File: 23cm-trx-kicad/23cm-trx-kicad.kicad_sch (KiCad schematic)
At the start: 62 parts, among them J1 LCD BACKLIGHT, J2 LCD I2C, Q1 BC547, Q2 BD138, Q3 BC557, SW1 RotaryEncoder_Switch, U1 ADF4153, U2 L78L09_SOT89, U3 LM741, U4 LM386

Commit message: Further schematic work
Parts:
- added X1: TCXO-13MHz, Oscillator:Oscillator_SMD_Abracon_ASE-4Pin_3.2x2.5mm, symbol Oscillator:ASE-xxxMHz
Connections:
- net GND: now also X1.2 (GND), X1.4 (Vdd)
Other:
- note added: "DRAW SYMBOL FOR MC3362"
- note removed: "DRAW SYMBOL FOR TCXO-13MHZ"
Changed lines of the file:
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@@
 	(wire
 		(pts
+			(xy 144.78 157.48) (xy 146.05 157.48)
+		)
+		(stroke
+			(width 0)
+			(type default)
+		)
+	)
+	(wire
+		(pts
 			(xy 67.31 68.58) (xy 67.31 77.47)
 		)
@@
 		)
 	)
+	(text "DRAW SYMBOL\nFOR MC3362"
+		(exclude_from_sim no)
+		(at 240.03 133.096 0)
+		(effects
+			(font
+				(size 1.27 1.27)
+			)
+		)
+	)
 	(text "POWER\nAMPLIFIER\n(PA)"
 		(exclude_from_sim no)
@@
 		)
 	)
-	(text "DRAW SYMBOL\nFOR TCXO-13MHZ"
-		(exclude_from_sim no)
-		(at 145.796 157.734 0)
-		(effects
-			(font
-				(size 1.27 1.27)
-			)
-		)
-	)
 	(text "USER MENU INPUT"
 		(exclude_from_sim no)
@@
 	(global_label "GND"
 		(shape passive)
+		(at 144.78 172.72 270)
+		(fields_autoplaced yes)
+		(effects
+			(font
+				(size 1.27 1.27)
+			)
+			(justify right)
+		)
+		(property "Intersheetrefs" "${INTERSHEET_REFS}"
+			(at 144.78 178.4644 90)
+			(effects
+				(font
+					(size 1.27 1.27)
+				)
+				(justify right)
+				(hide yes)
+			)
+		)
+	)
+	(global_label "GND"
+		(shape passive)
 		(at 55.88 92.71 270)
 		(fields_autoplaced yes)
@@
 		)
 	)
+	(global_label "GND"
+		(shape passive)
+		(at 146.05 157.48 0)
+		(fields_autoplaced yes)
+		(effects
+			(font
+				(size 1.27 1.27)
+			)
+			(justify left)
+		)
+		(property "Intersheetrefs" "${INTERSHEET_REFS}"
+			(at 151.7944 157.48 0)
+			(effects
+				(font
+					(size 1.27 1.27)
+				)
+				(justify left)
+				(hide yes)
+			)
+		)
+	)
 	(global_label "MCU-AUDIO"
 		(shape output)
@@
 					(unit 1)
 				)
+			)
+		)
+	)
+	(symbol
+		(lib_id "Oscillator:ASE-xxxMHz")
+		(at 144.78 165.1 0)
+		(unit 1)
+		(exclude_from_sim no)
+		(in_bom yes)
+		(on_board yes)
+		(dnp no)
+		(fields_autoplaced yes)
+		(property "Reference" "X1"
+			(at 157.48 158.7814 0)
+			(effects
+				(font
+					(size 1.27 1.27)
+				)
+			)
+		)
+		(property "Value" "TCXO-13MHz"
+			(at 157.48 161.3214 0)
+			(effects
+				(font
+					(size 1.27 1.27)
+				)
+			)
+		)
+		(property "Footprint" "Oscillator:Oscillator_SMD_Abracon_ASE-4Pin_3.2x2.5mm"
+			(at 162.56 173.99 0)
+			(effects
+				(font
+					(size 1.27 1.27)
+				)
+				(hide yes)
+			)
+		)
+		(property "Datasheet" ""
+			(at 142.24 165.1 0)
+			(effects
+				(font
+					(size 1.27 1.27)
+				)
+				(hide yes)
+			)
+		)
+		(property "Description" "3.3V CMOS SMD Crystal Clock Oscillator"
+			(at 144.78 165.1 0)
+			(effects
+				(font
+					(size 1.27 1.27)
+				)
+				(hide yes)
+			)
+		)
+		(pin "4"
+		)
+		(pin "1"
+		)
+		(pin "2"
+		)
+		(pin "3"
+		)
+		(instances
+			(project ""
+				(path "/02f64fd1-78db-4ce7-af00-a5ea9858044e"
+					(reference "X1")
+					(unit 1)
+				)

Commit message: More schematic
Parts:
- added C23: 100nF, symbol Device:C_Small
- added C24: 1nF, symbol Device:C_Small
- added D1: BZX84C3V3, Package_TO_SOT_SMD:SOT-23, symbol Diode:BZX84Cxx
- added R23: 470, symbol Device:R_Small_US
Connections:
- net 13.8V: now also R23.2
- net GND: now also C23.2, C24.2, D1.1 (A)
- net at C15.2, R20.1: now also C24.1
- net at X1.1 (EN): now also C23.1, D1.3 (K), R23.1
- net at X1.3 (OUT): now also C18.2
- net PLL-RF renamed PLL-RF-IN
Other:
- note added: "HOW IT WORKS (I THINK!): - THE OSCILLATOR CRYSTAL GENERATES A REFERENCE 13MHz SIGNAL THAT IS PASSED IN TO ADF4153. - USING AN EXTERNAL LOOP FILTER BETWEEN PINS x AND y, THE ADF4153 IMPLEMENTS A PHASE DETECTOR (PD) THAT COMPARES THE SIGNAL TO THAT RECEIVED ON PIN 6 (RFIN)."
- note added: "OUTPUT AUDIO POWER AMPLIFIER AND SPEAKER"
- note added: "PHASE LOCKED LOOP"
- note removed: "PHASE LOCK LOOP"
- note removed: "POWER AMPLIFIER AND SPEAKER"
- moved on the sheet: C15, C16, C17, C18, C19, C20, C21, C22, R20, R21, R22, SW1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

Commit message: Further schematic work
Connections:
- net at C15.2, C24.1: no longer R20.1
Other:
- note added: "HOW IT WORKS (I THINK!): - THE OSCILLATOR CRYSTAL GENERATES A REFERENCE 13MHz SIGNAL THAT IS PASSED IN TO ADF4153. - THE ADF4153 IS A FRACTIONAL-N FREQUENCY SYNTHESIZER THAT CONTAINS LOCAL OSCILLATORS AND A LOW NOISE DIGITAL FREQUENCY PHASE DETECTOR (PFD) FUNCTIONING AS THE PHASE DETECTOR (PD) WITHIN THE PHASE LOCKED LOOP. IT CHIEFLY COMPARES THE REFERENCE SIGNAL ON PIN 8 (REFIN) TO THAT RECEIVED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"
- note added: "VCO"
- note removed: "HOW IT WORKS (I THINK!): - THE OSCILLATOR CRYSTAL GENERATES A REFERENCE 13MHz SIGNAL THAT IS PASSED IN TO ADF4153. - USING AN EXTERNAL LOOP FILTER BETWEEN PINS x AND y, THE ADF4153 IMPLEMENTS A PHASE DETECTOR (PD) THAT COMPARES THE SIGNAL TO THAT RECEIVED ON PIN 6 (RFIN)."
- moved on the sheet: C10, C11, C15, C16, C17, C18, C19, C20, C21, C22, C23, C24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

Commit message: VCO
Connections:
- net CTCSS-TONE: no longer A1.14 (D11)
- net SPI-SCK: now reaches A1.16 (D13)
- net SPI-SCK: now also U1.11 (CLK)
- net CLK: no longer names the net of A1.19 (A0)
- net CLK: no longer U1.11 (CLK)
- net DAT: no longer names the net of A1.20 (A1)
- net DAT: no longer U1.12 (DATA)
- net LE: no longer names the net of A1.21 (A2)
- net LE: no longer U1.13 (LE)
- net PLL-RF-IN: no longer names the net of U1.6 (RFINA)
- new net SPI-MOSI: A1.14 (D11), U1.12 (DATA)
- new net SPI-SS-ADF4153: U1.13 (LE)
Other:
- moved on the sheet: C19, C20
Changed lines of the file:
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@@
 	)
 	(junction
-		(at 207.01 107.95)
-		(diameter 0)
-		(color 0 0 0 0)
-	)
-	(junction
 		(at 234.95 71.12)
 		(diameter 0)
@@
 	)
 	(junction
+		(at 212.09 107.95)
+		(diameter 0)
+		(color 0 0 0 0)
+	)
+	(junction
 		(at 194.31 135.89)
 		(diameter 0)
@@
 	(wire
 		(pts
+			(xy 120.65 113.03) (xy 120.65 132.08)
+		)
+		(stroke
+			(width 0)
+			(type default)
+		)
+	)
+	(wire
+		(pts
 			(xy 59.69 78.74) (xy 57.15 78.74)
 		)
@@
 	(wire
 		(pts
+			(xy 120.65 107.95) (xy 120.65 109.22)
+		)
+		(stroke
+			(width 0)
+			(type default)
+		)
+	)
+	(wire
+		(pts
 			(xy 124.46 46.99) (xy 133.35 46.99)
 		)
@@
 	(wire
 		(pts
+			(xy 120.65 107.95) (xy 144.78 107.95)
+		)
+		(stroke
+			(width 0)
+			(type default)
+		)
+	)
+	(wire
+		(pts
 			(xy 53.34 78.74) (xy 53.34 83.82)
 		)
@@
 	(wire
 		(pts
-			(xy 190.5 107.95) (xy 207.01 107.95)
+			(xy 190.5 107.95) (xy 212.09 107.95)
 		)
 		(stroke
@@
 	(wire
 		(pts
-			(xy 187.96 110.49) (xy 204.47 110.49)
+			(xy 187.96 110.49) (xy 208.28 110.49)
 		)
 		(stroke
@@
 	(wire
 		(pts
+			(xy 120.65 132.08) (xy 163.83 132.08)
+		)
+		(stroke
+			(width 0)
+			(type default)
+		)
+	)
+	(wire
+		(pts
 			(xy 68.58 30.48) (xy 77.47 30.48)
 		)
@@
 	(wire
 		(pts
-			(xy 204.47 135.89) (xy 194.31 135.89)
+			(xy 208.28 135.89) (xy 194.31 135.89)
 		)
 		(stroke
@@
 	(wire
 		(pts
-			(xy 124.46 107.95) (xy 144.78 107.95)
-		)
-		(stroke
-			(width 0)
-			(type default)
-		)
-	)
-	(wire
-		(pts
 			(xy 232.41 41.91) (xy 234.95 41.91)
 		)
@@
 	(wire
 		(pts
-			(xy 207.01 107.95) (xy 217.17 107.95)
+			(xy 212.09 107.95) (xy 222.25 107.95)
 		)
 		(stroke
@@
 	(wire
 		(pts
-			(xy 147.32 132.08) (xy 163.83 132.08)
-		)
-		(stroke
-			(width 0)
-			(type default)
-		)
-	)
-	(wire
-		(pts
-			(xy 204.47 110.49) (xy 204.47 135.89)
+			(xy 208.28 110.49) (xy 208.28 135.89)
 		)
 		(stroke
@@
 		)
 	)
-	(global_label "LE"
+	(global_label "SPI-SS-ADF4153"
 		(shape output)
-		(at 133.35 57.15 180)
+		(at 161.29 80.01 0)
 		(fields_autoplaced yes)
 		(effects
@@
 				(size 1.27 1.27)
 			)
-			(justify right)
+			(justify left)
 		)
 		(property "Intersheetrefs" "${INTERSHEET_REFS}"
-			(at 128.1877 57.15 0)
+			(at 181.2085 80.01 0)
 			(effects
 				(font
 					(size 1.27 1.27)
 				)
-				(justify right)
+				(justify left)
 				(hide yes)
 			)
@@
 		)
 	)
-	(global_label "CLK"
+	(global_label "SPI-SCK"
 		(shape input)
 		(at 187.96 120.65 0)
@@
 		)
 		(property "Intersheetrefs" "${INTERSHEET_REFS}"
-			(at 194.5133 120.65 0)
+			(at 199.3514 120.65 0)
 			(effects
 				(font
@@
 		)
 	)
-	(global_label "PLL-RF-IN"
-		(shape input)
-		(at 147.32 132.08 180)
-		(fields_autoplaced yes)
-		(effects
-			(font
-				(size 1.27 1.27)
-			)
-			(justify right)
-		)
-		(property "Intersheetrefs" "${INTERSHEET_REFS}"
-			(at 133.5699 132.08 0)
-			(effects
-				(font
-					(size 1.27 1.27)
-				)
-				(justify right)
-				(hide yes)
-			)
-		)
-	)
 	(global_label "TP"
 		(shape output)
@@
 	(global_label "CTCSS-TONE"
 		(shape output)
-		(at 158.75 64.77 0)
+		(at 161.29 77.47 0)
 		(fields_autoplaced yes)
 		(effects
@@
 		)
 		(property "Intersheetrefs" "${INTERSHEET_REFS}"
-			(at 174.0118 64.77 0)
+			(at 176.5518 77.47 0)
 			(effects
 				(font
@@
 	(global_label "GND"
 		(shape passive)
-		(at 217.17 113.03 270)
+		(at 222.25 113.03 270)
 		(fields_autoplaced yes)
 		(effects
@@
 		)
 		(property "Intersheetrefs" "${INTERSHEET_REFS}"
-			(at 217.17 118.7744 90)
+			(at 222.25 118.7744 90)
 			(effects
 				(font
@@
 		)
 	)
-	(global_label "LE"
-		(shape input)
-		(at 187.96 115.57 0)
-		(fields_autoplaced yes)
-		(effects
-			(font
-				(size 1.27 1.27)
-			)
-			(justify left)
-		)
-		(property "Intersheetrefs" "${INTERSHEET_REFS}"
-			(at 193.1223 115.57 0)
-			(effects
-				(font
-					(size 1.27 1.27)
-				)
-				(justify left)
-				(hide yes)
-			)
-		)
-	)
 	(global_label "GND"
 		(shape passive)
@@
 	(global_label "GND"
 		(shape passive)
-		(at 207.01 113.03 270)
+		(at 212.09 113.03 270)
 		(fields_autoplaced yes)
 		(effects
@@
 		)
 		(property "Intersheetrefs" "${INTERSHEET_REFS}"
-			(at 207.01 118.7744 90)
+			(at 212.09 118.7744 90)
 			(effects
 				(font
@@
 		)
 	)
-	(global_label "DAT"
+	(global_label "SPI-MOSI"
 		(shape input)
 		(at 187.96 118.11 0)
@@
 		)
 		(property "Intersheetrefs" "${INTERSHEET_REFS}"
-			(at 194.2714 118.11 0)
+			(at 200.1981 118.11 0)
 			(effects
 				(font
@@
 		)
 	)
-	(global_label "DAT"
+	(global_label "SPI-MOSI"
 		(shape output)
-		(at 133.35 54.61 180)
+		(at 158.75 64.77 0)
 		(fields_autoplaced yes)
 		(effects
@@
 				(size 1.27 1.27)
 			)
-			(justify right)
+			(justify left)
 		)
 		(property "Intersheetrefs" "${INTERSHEET_REFS}"
-			(at 127.0386 54.61 0)
+			(at 170.9881 64.77 0)
 			(effects
 				(font
 					(size 1.27 1.27)
 				)
-				(justify right)
+				(justify left)
 				(hide yes)
 			)
@@
 		)
 	)
+	(global_label "SPI-SS-ADF4153"
+		(shape input)
+		(at 187.96 115.57 0)
+		(fields_autoplaced yes)
+		(effects
+			(font
+				(size 1.27 1.27)
+			)
+			(justify left)
+		)
+		(property "Intersheetrefs" "${INTERSHEET_REFS}"
+			(at 207.8785 115.57 0)
+			(effects
+				(font
+					(size 1.27 1.27)
+				)
+				(justify left)
+				(hide yes)
+			)
+		)
+	)
 	(global_label "VIN-15V-33V"
 		(shape input)
@@
 		)
 	)
-	(global_label "CLK"
+	(global_label "SPI-SCK"
 		(shape output)
-		(at 133.35 52.07 180)
+		(at 158.75 69.85 0)
 		(fields_autoplaced yes)
 		(effects
@@
 				(size 1.27 1.27)
 			)
-			(justify right)
+			(justify left)
 		)
 		(property "Intersheetrefs" "${INTERSHEET_REFS}"
-			(at 126.7967 52.07 0)
+			(at 170.1414 69.85 0)
 			(effects
 				(font
 					(size 1.27 1.27)
 				)
-				(justify right)
+				(justify left)
 				(hide yes)
 			)
@@
 	(symbol
 		(lib_id "Device:C_Small")
-		(at 207.01 110.49 0)
+		(at 212.09 110.49 0)
 		(unit 1)
 		(exclude_from_sim no)
@@
 		(dnp no)
 		(property "Reference" "C19"
-			(at 209.55 109.2262 0)
+			(at 214.63 109.2262 0)
 			(effects
 				(font
@@
 		)
 		(property "Value" "10nF"
-			(at 209.55 111.7662 0)
+			(at 214.63 111.7662 0)
 			(effects
 				(font
@@
 		)
 		(property "Footprint" ""
-			(at 207.01 110.49 0)
+			(at 212.09 110.49 0)
 			(effects
 				(font
@@
 		)
 		(property "Datasheet" "~"
-			(at 207.01 110.49 0)
+			(at 212.09 110.49 0)
 			(effects
 				(font
@@
 		)
 		(property "Description" "Unpolarized capacitor, small symbol"
-			(at 207.01 110.49 0)
+			(at 212.09 110.49 0)
 			(effects
 				(font
@@
 	(symbol
 		(lib_id "Device:C_Polarized_Small")
-		(at 217.17 110.49 0)
+		(at 222.25 110.49 0)
 		(unit 1)
 		(exclude_from_sim no)
@@
 		(fields_autoplaced yes)
 		(property "Reference" "C20"
-			(at 219.71 108.6738 0)
+			(at 224.79 108.6738 0)
 			(effects
 				(font
@@
 		)
 		(property "Value" "47uF"
-			(at 219.71 111.2138 0)
+			(at 224.79 111.2138 0)
 			(effects
 				(font
@@
 		)
 		(property "Footprint" ""
-			(at 217.17 110.49 0)
+			(at 222.25 110.49 0)
 			(effects
 				(font
@@
 		)
 		(property "Datasheet" "~"
-			(at 217.17 110.49 0)
+			(at 222.25 110.49 0)
 			(effects
 				(font
@@
 		)
 		(property "Description" "Polarized capacitor, small symbol"
-			(at 217.17 110.49 0)
+			(at 222.25 110.49 0)
 			(effects
 				(font

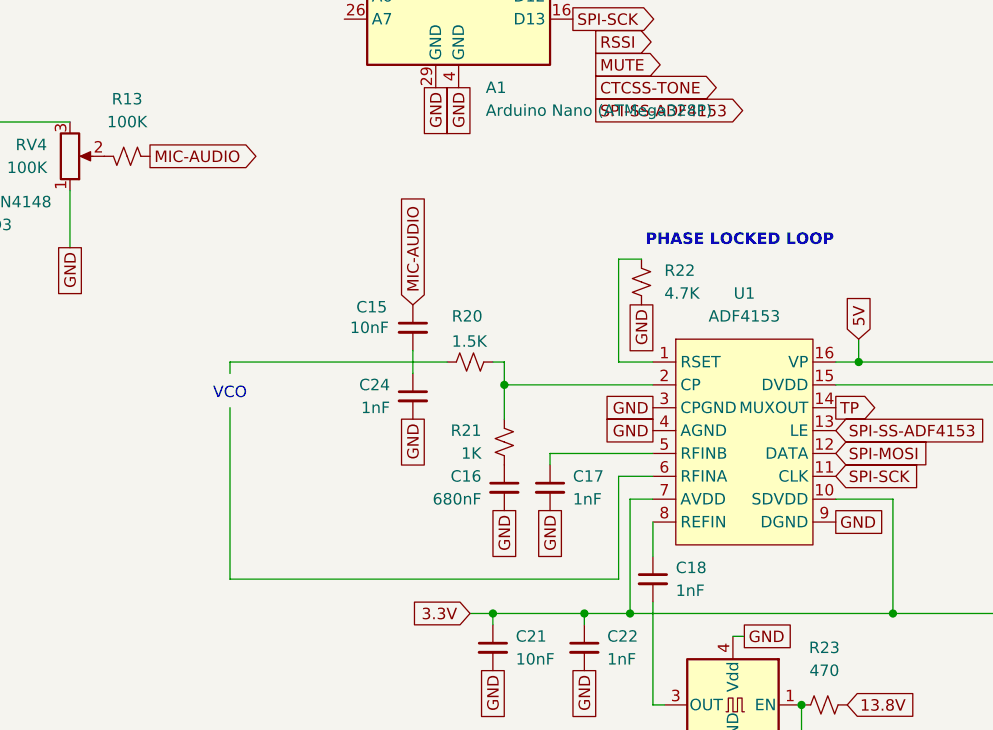
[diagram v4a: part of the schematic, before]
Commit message: Label PLL portions
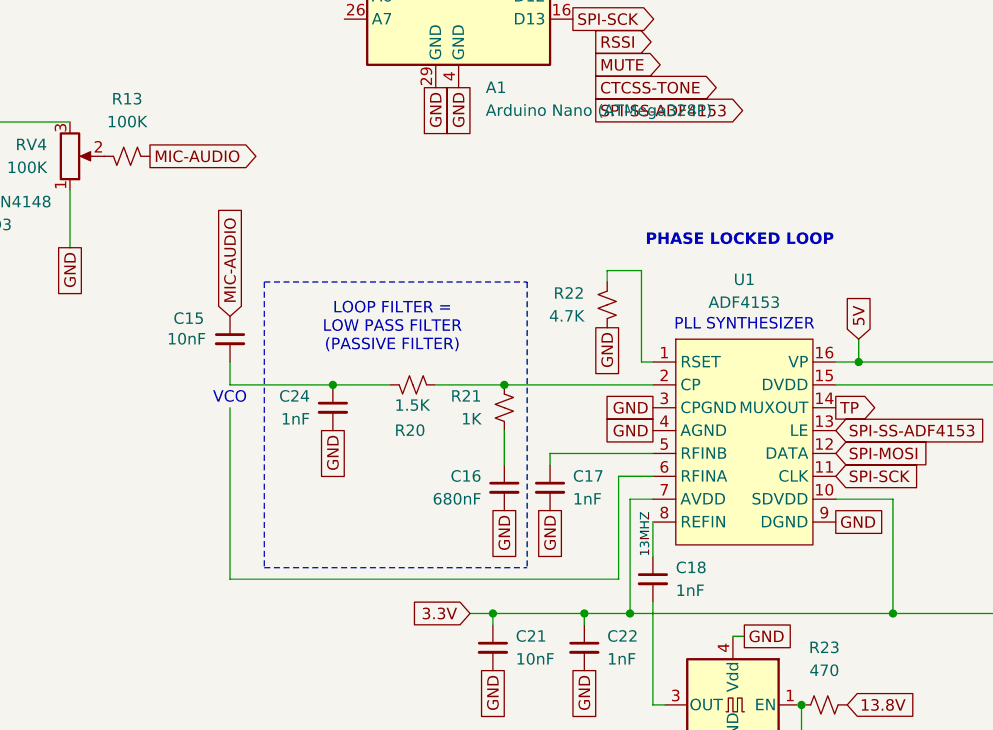
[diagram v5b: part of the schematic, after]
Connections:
- net at C15.2, C24.1: now also R20.1
- net 13MHZ: now reaches C18.1, U1.8 (REFIN)
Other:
- note added: "LOOP FILTER = LOW PASS FILTER (PASSIVE FILTER)"
- note added: "PLL SYNTHESIZER"
- moved on the sheet: C15, C24, R20, R21, R22

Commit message: VCO notes
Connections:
- net SPI-MISO: now reaches A1.15 (D12)
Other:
- note added: "DRAW SYMBOL FOR VCO"
- note added: "NOTING HAMS WANT THE 1240-1300 MHz RANGE: POSSIBLE VCOs @ 1100-1350MHz: - ALPS-1679C (NO RECORD) - UNOBTAINIUM - Y17C (GERMAN RECORD AT https://www.mikrocontroller.net/topic/353869 SUGGESTS 0.5V-9V RANGE NAVIGATES 1087-1345MHz) - UNOBTAINIUM OTHERS (GOOD): - M1200 (NOMINAL 1200MHz, +0-5V NAVIGATES 1150-1350MHz) - 6RMB @ https://www.fresend.com/productinfo/647892.html [CURRENT PRODUCT] - RFINT INN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"
- moved on the sheet: A1, C1, R2

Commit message: Many component definitions
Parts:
- C1, C10, C2, C23, C3, C4, C9: footprint (none) -> Capacitor_SMD:C_0805_2012Metric; LCSC Part # (none) -> C28233; MPN (none) -> CL21B104KCFNNNE; Manufacturer (none) -> Samsung
- C11: footprint (none) -> Capacitor_SMD:C_0805_2012Metric; LCSC Part # (none) -> C28323; MPN (none) -> CL21B105KBFNNNE; Manufacturer (none) -> Samsung
- C12: footprint (none) -> Capacitor_SMD:C_0805_2012Metric; LCSC Part # (none) -> C5378; MPN (none) -> CL21B224KBFNNNE; Manufacturer (none) -> Samsung
- C13: footprint (none) -> Capacitor_SMD:CP_Elec_10x10; LCSC Part # (none) -> C116211; MPN (none) -> UCD1H221MNL1GS; Manufacturer (none) -> Nichicon
- C14: footprint (none) -> Capacitor_SMD:C_0805_2012Metric; LCSC Part # (none) -> C53134; MPN (none) -> CL21B473KBCNNNC; Manufacturer (none) -> Samsung
- C17, C18, C22, C24: footprint (none) -> Capacitor_SMD:C_1206_3216Metric; LCSC Part # (none) -> C9196; MPN (none) -> 1206B102K202NT; Manufacturer (none) -> Fenghua
- C19, C21, C8: footprint (none) -> Capacitor_SMD:C_0805_2012Metric; LCSC Part # (none) -> C1710; MPN (none) -> CL21B103KBANNNC; Manufacturer (none) -> Samsung
- C20: footprint (none) -> Capacitor_SMD:C_1206_3216Metric; LCSC Part # (none) -> C96123; MPN (none) -> CL31A476MPHNNNE; Manufacturer (none) -> Samsung
- C5, C6, C7: footprint (none) -> Capacitor_SMD:C_0603_1608Metric; LCSC Part # (none) -> C1613; MPN (none) -> CL10B332KB8NNNC; Manufacturer (none) -> Samsung
- D1: LCSC Part # (none) -> C19077467; MPN (none) -> BZX84C3V3; Manufacturer (none) -> hongjiacheng
- D2, D3: LCSC Part # (none) -> C2128; MPN (none) -> 1N4148WS
- R1: footprint (none) -> Resistor_SMD:R_0805_2012Metric; LCSC Part # (none) -> C17415; MPN (none) -> 0805W8F100JT5E; Manufacturer (none) -> Uniroyal
- R10: value 2.2M -> 27K; footprint (none) -> Resistor_SMD:R_0805_2012Metric; LCSC Part # (none) -> C17593; MPN (none) -> 0805W8F2702T5E; Manufacturer (none) -> Uniroyal
- R11: footprint (none) -> Resistor_SMD:R_0805_2012Metric; LCSC Part # (none) -> C17475; MPN (none) -> 0805W8F1502T5E; Manufacturer (none) -> Uniroyal
- R13: footprint (none) -> Resistor_SMD:R_0805_2012Metric; LCSC Part # (none) -> C149504; MPN (none) -> 0805W8F1003T5E; Manufacturer (none) -> Uniroyal
- R14, R15: footprint (none) -> Resistor_SMD:R_0805_2012Metric; LCSC Part # (none) -> C17470; MPN (none) -> 0805W8F1503T5E; Manufacturer (none) -> Uniroyal
- R2: footprint (none) -> Resistor_SMD:R_0805_2012Metric; LCSC Part # (none) -> C17673; MPN (none) -> 0805W8F4701T5E; Manufacturer (none) -> Uniroyal
- R3, R4, R5, R6, R7, R8: footprint (none) -> Resistor_SMD:R_0805_2012Metric; LCSC Part # (none) -> C17593; MPN (none) -> 0805W8F2702T5E; Manufacturer (none) -> Uniroyal
- R9: value 12 -> 10; footprint (none) -> Resistor_SMD:R_0805_2012Metric; LCSC Part # (none) -> C17415; MPN (none) -> 0805W8F100JT5E; Manufacturer (none) -> Uniroyal
- U2: LCSC Part # (none) -> C52103; MPN (none) -> L78L09ABUTR; Manufacturer (none) -> STMicro
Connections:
- net GND: now also C17.1; no longer C17.2
- net MCU-AUDIO: now also R10.2; no longer R10.1
- net at D2.1 (K), D3.2 (A), RV4.3: now also C9.2; no longer C9.1
- net at R11.1, U3.6: now also C9.1; no longer C9.2
- net at C4.1, R6.2: now also R10.1; no longer R10.2
- net at U1.5 (RFINB): now also C17.2; no longer C17.1
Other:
- note added: "23CM TRANSCEIVER"
- note added: "PARTIAL DRAFT"
- note added: "THIS WAS 12 IN THE ORIGINAL DESIGN, BUT IT WAS MORE LOGICAL TO USE 10 HERE TO REDUCE THE COMPONENT COUNT. SHOULD EQUATE."
